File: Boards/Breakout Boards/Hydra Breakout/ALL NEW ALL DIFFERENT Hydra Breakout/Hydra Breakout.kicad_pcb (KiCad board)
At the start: 2 copper layers, 480.7 x 176.7 mm, 265 parts, among them IC6 INA2181A4IDSQR, IC7 INA181A4QDCKRQ1, IC8 PCA9306GM,125, J1 Conn_01x01_Socket, J11 Conn_01x01_Socket, J12 Conn_01x01_Socket, J13 Conn_01x01_Socket, J14 Conn_01x01_Socket, J15 Conn_01x01_Socket, J16 Conn_01x01_Socket, J17 Conn_01x01_Socket, J18 Conn_01x01_Socket, J2 Conn_01x01_Socket, J3 Conn_01x01_Socket, J4 Conn_01x01_Socket, J5 Conn_01x01_Socket, J6 Conn_01x01_Socket, J7 BM03B-SRSS-TBLFSN, J8 Conn_01x01_Socket, J9 Conn_01x01_Socket, Q2 2N7002H6327XTSA2, Q3 2N7002H6327XTSA2, Q5 BC857CMB_315, Q6 BC857CMB_315, Q7 BC857CMB_315, U1 SC0915, U10 STLM20DD9F, U13 LM61460AASQRJRRQ1, U14 LM61460AASQRJRRQ1, U2 MAX31856MUD+T, U3 MAX31856MUD+T, U4 LM61460AASQRJRRQ1, U5 SQJA36EP-T1_GE3, U6 THVD2410VDRCR, U7 MAX31856MUD+T, U8 max11614eee+, U9 SQJA36EP-T1_GE3

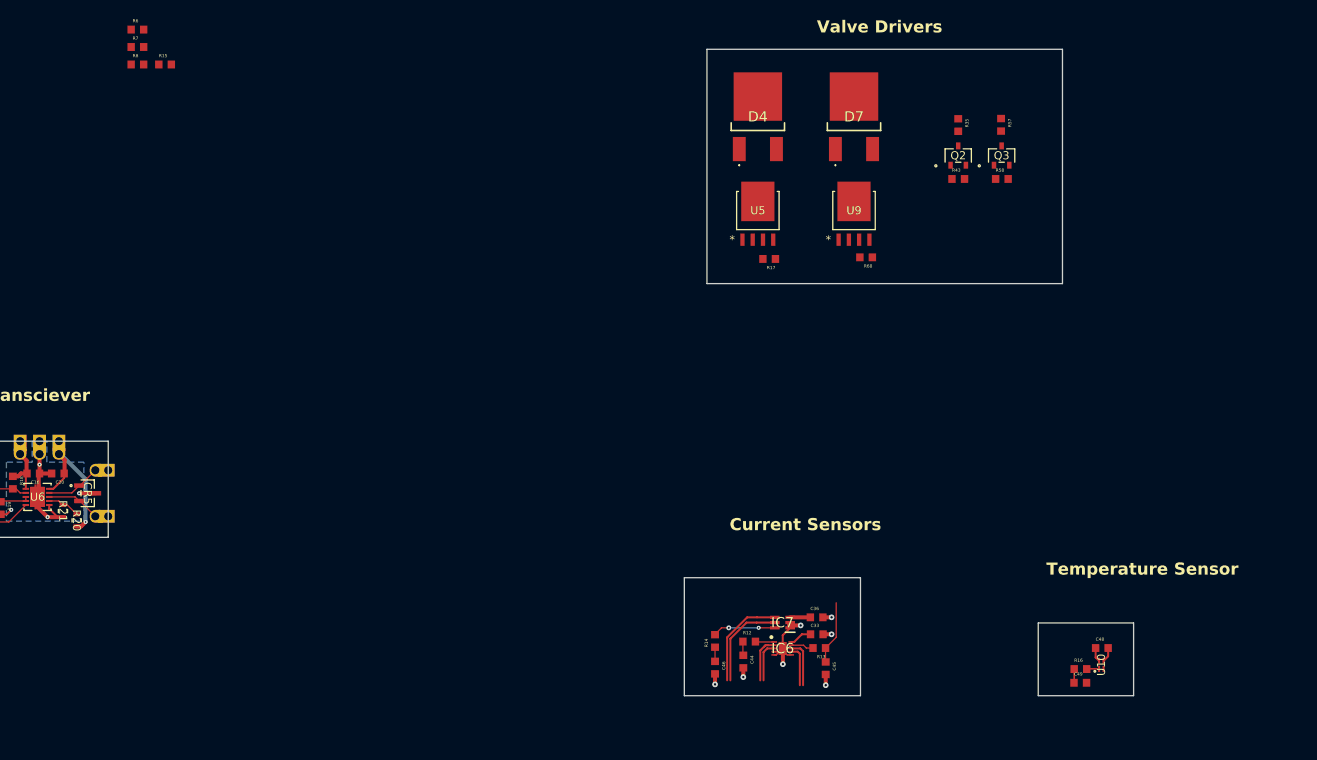
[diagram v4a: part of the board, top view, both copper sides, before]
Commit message: Design da Hydra Breakout (Part 5)
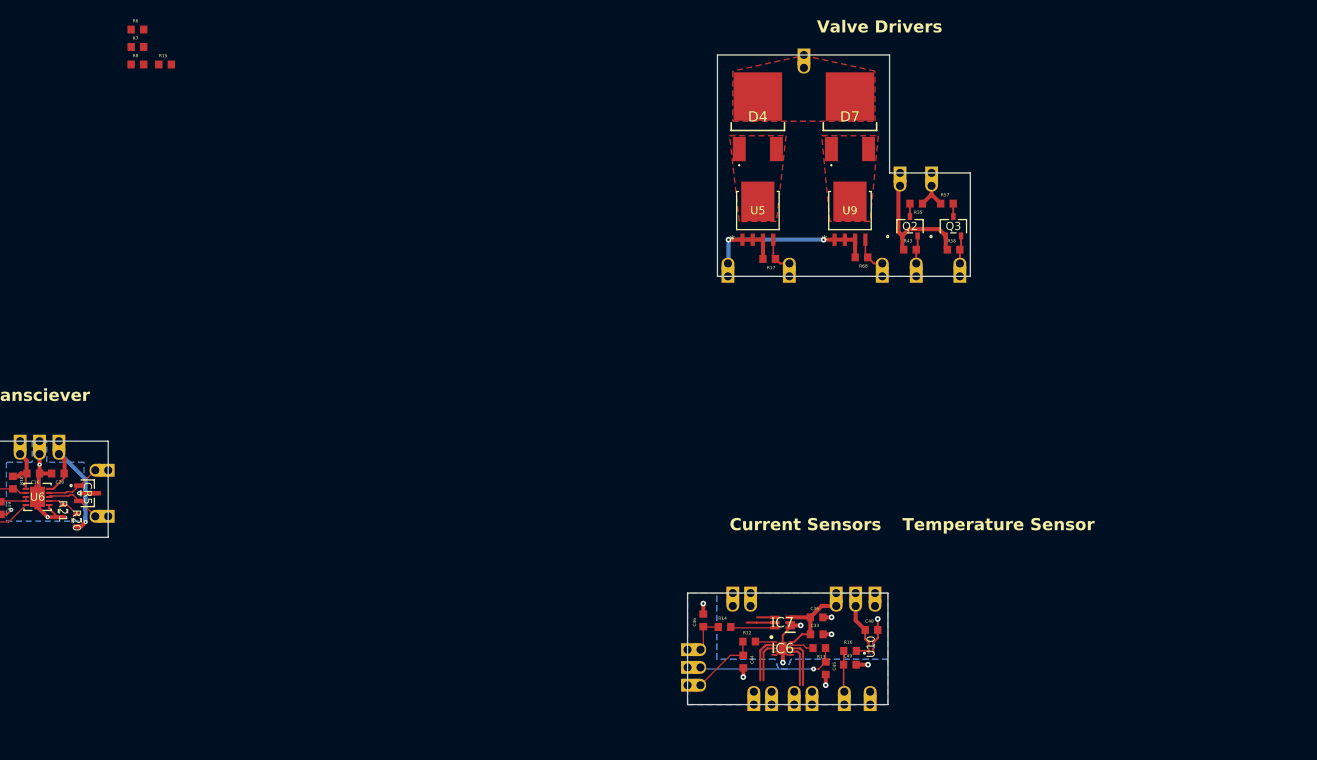
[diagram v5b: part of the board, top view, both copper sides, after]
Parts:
- added REF**: Pico_01pin, Pico_Conn1x1:Pico_01pin, F.Cu at (306.2, 180.4)
- added REF**: Pico_01pin, Pico_Conn1x1:Pico_01pin, F.Cu at (334.8, 118.6)
- added REF**: Pico_01pin, Pico_Conn1x1:Pico_01pin, F.Cu at (328.7, 128.2)
- added REF**: Pico_01pin, Pico_Conn1x1:Pico_01pin, F.Cu at (315.0, 181.2)
- added REF**: Pico_01pin, Pico_Conn1x1:Pico_01pin, F.Cu at (325.4, 170.6)
- added REF**: Pico_01pin, Pico_Conn1x1:Pico_01pin, F.Cu at (312.4, 170.6)
- added REF**: Pico_01pin, Pico_Conn1x1:Pico_01pin, F.Cu at (319.0, 104.0)
- added REF**: Pico_01pin, Pico_Conn1x1:Pico_01pin, F.Cu at (320.0, 181.2)
- added REF**: Pico_01pin, Pico_Conn1x1:Pico_01pin, F.Cu at (324.0, 181.2)
- added REF**: Pico_01pin, Pico_Conn1x1:Pico_01pin, F.Cu at (317.2, 128.2)
- added REF**: Pico_01pin, Pico_Conn1x1:Pico_01pin, F.Cu at (330.9, 118.6)
- added REF**: Pico_01pin, Pico_Conn1x1:Pico_01pin, F.Cu at (310.2, 170.6)
- added REF**: Pico_01pin, Pico_Conn1x1:Pico_01pin, F.Cu at (306.2, 176.0)
- added REF**: Pico_01pin, Pico_Conn1x1:Pico_01pin, F.Cu at (338.3, 128.2)
- added REF**: Pico_01pin, Pico_Conn1x1:Pico_01pin, F.Cu at (309.6, 128.2)
- added REF**: Pico_01pin, Pico_Conn1x1:Pico_01pin, F.Cu at (332.9, 128.2)
- added REF**: Pico_01pin, Pico_Conn1x1:Pico_01pin, F.Cu at (306.2, 178.2)
- added REF**: Pico_01pin, Pico_Conn1x1:Pico_01pin, F.Cu at (317.8, 181.2)
- added REF**: Pico_01pin, Pico_Conn1x1:Pico_01pin, F.Cu at (327.8, 170.6)
- added REF**: Pico_01pin, Pico_Conn1x1:Pico_01pin, F.Cu at (312.8, 181.2)
- added REF**: Pico_01pin, Pico_Conn1x1:Pico_01pin, F.Cu at (323.0, 170.6)
- added REF**: Pico_01pin, Pico_Conn1x1:Pico_01pin, F.Cu at (327.2, 181.2)
- moved C48 28.6 mm to (327.4, 173.6)
- moved C49 28.6 mm to (324.7, 177.9)
- moved R16 28.6 mm to (324.7, 176.2)
- moved U10 28.6 mm to (327.3, 175.6)
- moved R57 11.8 mm to (336.7, 120.8), turned to 0 degrees
- moved R35 11.0 mm to (332.9, 120.8), turned to 180 degrees
- moved Q2 10.6 mm to (332.1, 123.6)
- moved R43 10.6 mm to (332.1, 126.5)
- moved Q3 10.6 mm to (337.5, 123.6)
- moved R58 10.6 mm to (337.5, 126.5)
- moved C46 6.03 mm to (306.6, 172.4), turned to 90 degrees
- moved R14 2.09 mm to (309.2, 173.2), turned to 0 degrees
- moved R68 0.57 mm to (326.1, 127.5)
- moved D7 0.50 mm to (324.7, 109.8)
- moved U9 0.50 mm to (324.7, 121.7)
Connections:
- C_VCC3 pad 1: /Power Unit/DC.DC3 VCC -> GNDA
- C_VCC3 pad 2: GNDA -> /Power Unit/DC.DC3 VCC
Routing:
- net GND: track 70.7 -> 100.1 mm, vias 23 -> 26
- net +3.3V: track 52.1 -> 71.7 mm
- net /Power Unit/V3 DP: track 12.2 -> 2.20 mm
- net /Sensor Unit/ADC2 Sense: track 11.3 -> 21.1 mm, vias 0 -> 1
- net /Sensor Unit/ADC1 Sense: track 5.81 -> 12.6 mm
- net /Purge Valve Enable: track 0.00 -> 4.45 mm
- net /Solenoid Valve Enable: track 0.00 -> 4.45 mm
- net /Servo_IN1 PWM: track 0.00 -> 3.48 mm
- net /Servo_IN2 PWM: track 0.00 -> 3.47 mm
- net /Sensor Unit/Temp_Sense: track 1.71 -> 5.08 mm
- net /Sensor Unit/ADC3 Sense: track 5.56 -> 8.56 mm
- net /Sensor Unit/5V_Sense: track 7.78 -> 5.49 mm, vias 2 -> 0
- net +5V: track 79.6 -> 81.8 mm
- net /Servo_OUT2 PWM: track 0.00 -> 1.62 mm
- net /Servo_OUT1 PWM: track 0.00 -> 1.61 mm
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- added copper zone on F.Cu, net +12V
- added copper zone on F.Cu, net /Main Solenoid Valve
- added copper zone on F.Cu, net /Purge Solenoid Valve
- added copper zone on B.Cu, net GNDA
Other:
- outline, holes or cut-outs redrawn
